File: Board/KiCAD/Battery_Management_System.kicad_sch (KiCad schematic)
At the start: 5 parts, among them J4 Conn_01x02, J5 Conn_01x03, J6 Conn_01x03, J7 Conn_01x05, J8 Conn_01x02

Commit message: Add files via upload
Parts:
- removed J4: Conn_01x02, symbol Connector_Generic:Conn_01x02
- removed J6: Conn_01x03, symbol Connector_Generic:Conn_01x03
- added J1: Conn_01x06_Socket, symbol Connector:Conn_01x06_Socket
- added J9: Conn_01x02, symbol Connector_Generic:Conn_01x02
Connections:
- net Charge Control/VBus: now also J9.1 (Pin_1)
- net GND: now also J1.6 (Pin_6), J9.2 (Pin_2)
- net Microcontroller/USART1_RX: now also J1.2 (Pin_2)
- net Microcontroller/USART1_TX: now also J1.3 (Pin_3)
- new net 3.3V: J1.4 (Pin_4)
- new net NC: J1.1 (Pin_1), J1.5 (Pin_5)
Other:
- sheet Charge Control ports: added none; removed PGND
- sheet Microcontroller ports: added Thermistor C1, Thermistor C2, Thermistor C3, Thermistor C4; removed none
- note added: "External Power In Usercase: 24V/4A"
- note added: "Host Microcontroller"
- note added: "Power out to Load"
- note added: "USB to Serial Breaktout FT232RL"
- note removed: "External Power In Voltage range? Current range?"
- note removed: "Power out, right?"
- note removed: "To Host, right?"
- note removed: "What is this, debug?"
- note removed: "What voltage? Current?"
- moved on the sheet: J5, J7, J8

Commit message: Add files via upload
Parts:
- J1: footprint (none) -> Connector_PinHeader_1.00mm:PinHeader_1x06_P1.00mm_Vertical
- J5: footprint (none) -> Connector_PinHeader_1.00mm:PinHeader_1x03_P1.00mm_Vertical
- J7: footprint (none) -> Connector_PinHeader_1.00mm:PinHeader_1x05_P1.00mm_Vertical
- J8, J9: footprint (none) -> Connector_PinHeader_1.00mm:PinHeader_1x02_P1.00mm_Vertical
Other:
- moved on the sheet: J1, J5, J7, J8, J9

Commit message: Add files via upload
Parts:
- J1: footprint Connector_PinHeader_1.00mm:PinHeader_1x06_P1.00mm_Vertical -> Connector_PinHeader_2.54mm:PinHeader_1x06_P2.54mm_Vertical
- J5: footprint Connector_PinHeader_1.00mm:PinHeader_1x03_P1.00mm_Vertical -> Connector_PinHeader_2.54mm:PinHeader_1x03_P2.54mm_Vertical
- J7: footprint Connector_PinHeader_1.00mm:PinHeader_1x05_P1.00mm_Vertical -> Connector_PinHeader_2.54mm:PinHeader_1x05_P2.54mm_Vertical
- J8, J9: footprint Connector_PinHeader_1.00mm:PinHeader_1x02_P1.00mm_Vertical -> Connector_PinHeader_2.54mm:PinHeader_1x02_P2.54mm_Vertical
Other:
- note removed: "So you're going to use castellated vias, right? How do you do those? A footprint with multiple connector icons?"
- note removed: "User MUST place batteries starting at Cell 1. Unused cells MUST be bypassed on carrier PCB."
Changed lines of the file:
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@@
-		)
-	)
-	(text "User MUST place batteries starting at Cell 1.\nUnused cells MUST be bypassed on carrier PCB.\n"
-		(exclude_from_sim no)
-		(at 232.41 123.19 0)
-		(effects
-			(font
-				(size 1.778 1.778)
-			)
 		)
 	)
@@
 		(exclude_from_sim no)
 		(at 195.58 124.46 0)
-		(effects
-			(font
-				(size 1.27 1.27)
-			)
-		)
-	)
-	(text "So you're going to use castellated vias, right? \nHow do you do those? A footprint with multiple connector icons?"
-		(exclude_from_sim no)
-		(at 121.92 156.21 0)
 		(effects
 			(font
@@
 			)
 		)
-		(property "Footprint" "Connector_PinHeader_1.00mm:PinHeader_1x03_P1.00mm_Vertical"
+		(property "Footprint" "Connector_PinHeader_2.54mm:PinHeader_1x03_P2.54mm_Vertical"
 			(at 62.23 87.63 0)
 			(effects
@@
 			)
 		)
-		(property "Footprint" "Connector_PinHeader_1.00mm:PinHeader_1x06_P1.00mm_Vertical"
+		(property "Footprint" "Connector_PinHeader_2.54mm:PinHeader_1x06_P2.54mm_Vertical"
 			(at 60.96 105.41 0)
 			(effects
@@
 			)
 		)
-		(property "Footprint" "Connector_PinHeader_1.00mm:PinHeader_1x02_P1.00mm_Vertical"
+		(property "Footprint" "Connector_PinHeader_2.54mm:PinHeader_1x02_P2.54mm_Vertical"
 			(at 190.5 55.88 0)
 			(effects
@@
 			)
 		)
-		(property "Footprint" "Connector_PinHeader_1.00mm:PinHeader_1x05_P1.00mm_Vertical"
+		(property "Footprint" "Connector_PinHeader_2.54mm:PinHeader_1x05_P2.54mm_Vertical"
 			(at 189.23 120.65 0)
 			(effects
@@
 			)
 		)
-		(property "Footprint" "Connector_PinHeader_1.00mm:PinHeader_1x02_P1.00mm_Vertical"
+		(property "Footprint" "Connector_PinHeader_2.54mm:PinHeader_1x02_P2.54mm_Vertical"
 			(at 63.5 59.69 0)
 			(effects

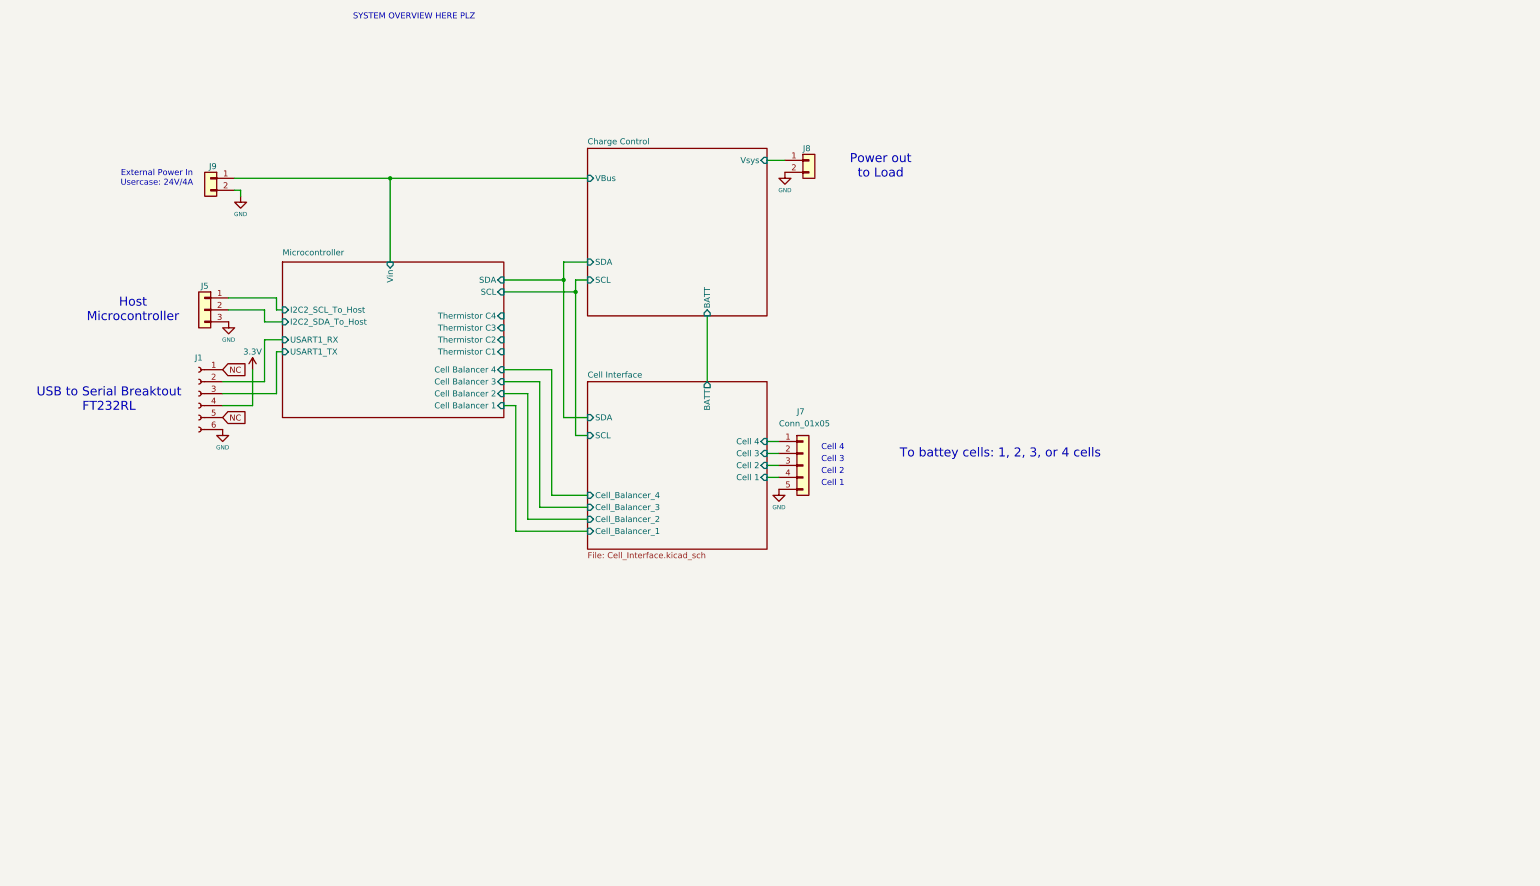
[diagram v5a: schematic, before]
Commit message: Schematic: - Fixed FDI plug - Added thermistor connectors - Added a bunch of NCs using KiCAD NC tool - Added filter cap back into battery current shunt - Added bypass cap to LTC - Removed Cell 4 INA260 because the LTC does current, voltage of that top cell! Board Layout: - Chewed out team for not reading the BQ's datasheet, specifically Section 11 - Relayed out power stream using Section 11 as a refernce - Changed some footprints, mostly reducing size to 0603 - Positioned things optimally given what I thought made sense (dangerous, I know) - Fixed ground planes Other: - Removed PRL and CACHE files from the repo.
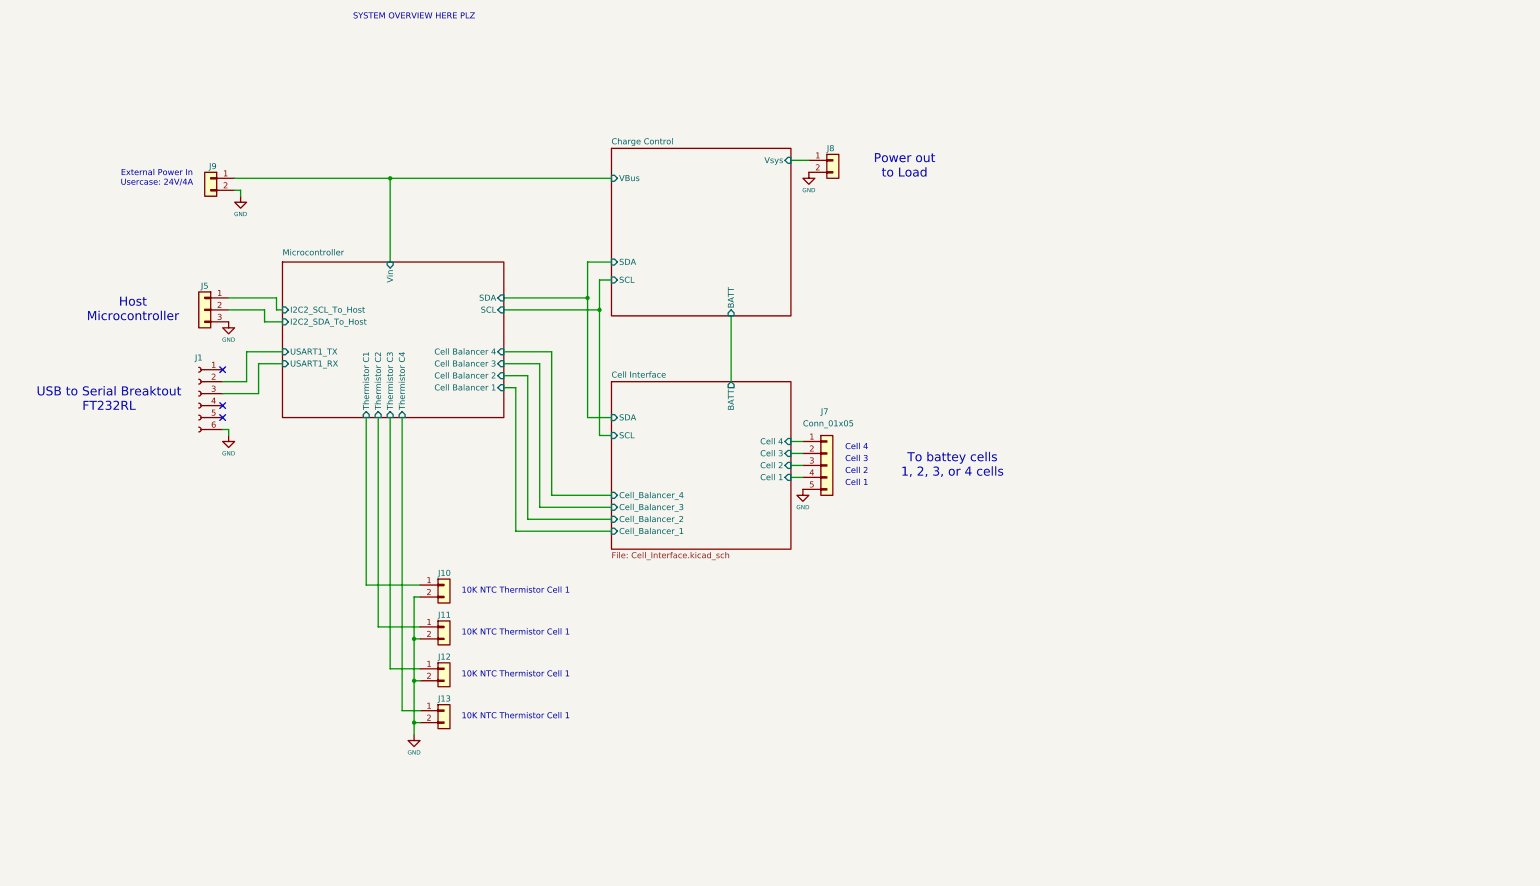
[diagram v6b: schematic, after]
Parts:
- added J10, J11, J12, J13: Conn_01x02, Connector_PinHeader_2.54mm:PinHeader_1x02_P2.54mm_Vertical, symbol Connector_Generic:Conn_01x02
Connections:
- net GND: now also J10.2 (Pin_2), J11.2 (Pin_2), J12.2 (Pin_2), J13.2 (Pin_2)
- net Microcontroller/Thermistor C1: now also J10.1 (Pin_1)
- net Microcontroller/Thermistor C2: now also J11.1 (Pin_1)
- net Microcontroller/Thermistor C3: now also J12.1 (Pin_1)
- net Microcontroller/Thermistor C4: now also J13.1 (Pin_1)
- net Microcontroller/USART1_RX: now also J1.3 (Pin_3); no longer J1.2 (Pin_2)
- net Microcontroller/USART1_TX: now also J1.2 (Pin_2); no longer J1.3 (Pin_3)
- net 3.3V: no longer names the net of J1.4 (Pin_4)
- net NC: no longer names the net of J1.1 (Pin_1)
- net NC: no longer J1.5 (Pin_5)
- no-connect marks 0 -> 3
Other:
- note added: "10K NTC Thermistor Cell 1"
- note added: "To battey cells 1, 2, 3, or 4 cells"
- note removed: "To battey cells: 1, 2, 3, or 4 cells"
- moved on the sheet: J7, J8

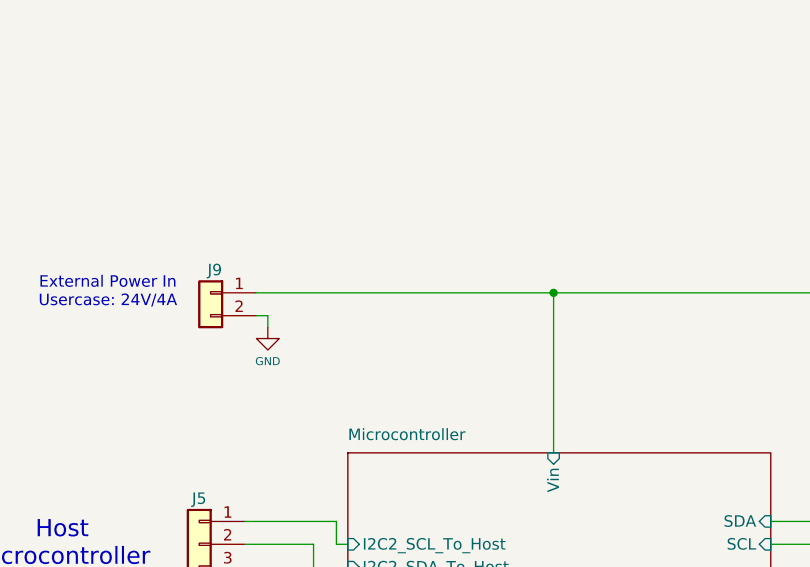
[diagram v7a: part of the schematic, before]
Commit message: Added example test point
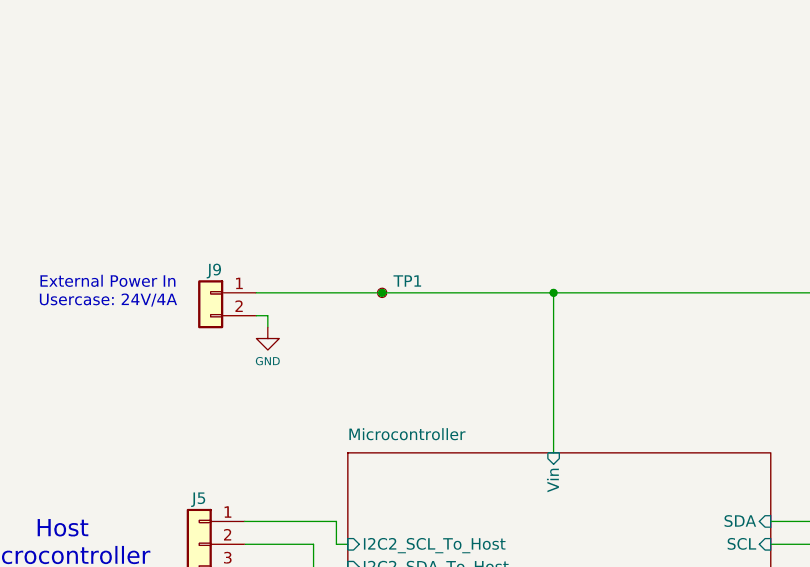
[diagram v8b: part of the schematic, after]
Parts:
- added TP1: TestPoint_Small, TestPoint:TestPoint_THTPad_1.0x1.0mm_Drill0.5mm, symbol Connector:TestPoint_Small
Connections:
- net Charge Control/VBus: now also TP1.1
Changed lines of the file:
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@@
+	)
+	(junction
+		(at 82.55 59.69)
+		(diameter 0)
+		(color 0 0 0 0)
 	)
 	(junction
@@
 	(wire
 		(pts
-			(xy 68.58 59.69) (xy 101.6 59.69)
+			(xy 68.58 59.69) (xy 82.55 59.69)
 		)
 		(stroke
@@
 		(pts
 			(xy 106.68 148.59) (xy 106.68 157.48)
+		)
+		(stroke
+			(width 0)
+			(type default)
+		)
+	)
+	(wire
+		(pts
+			(xy 82.55 59.69) (xy 101.6 59.69)
 		)
 		(stroke
@@
 					(unit 1)
 				)
+			)
+		)
+	)
+	(symbol
+		(lib_id "Connector:TestPoint_Small")
+		(at 82.55 59.69 0)
+		(unit 1)
+		(exclude_from_sim no)
+		(in_bom no)
+		(on_board yes)
+		(dnp no)
+		(fields_autoplaced yes)
+		(property "Reference" "TP1"
+			(at 83.82 58.4199 0)
+			(effects
+				(font
+					(size 1.27 1.27)
+				)
+				(justify left)
+			)
+		)
+		(property "Value" "TestPoint_Small"
+			(at 83.82 60.9599 0)
+			(effects
+				(font
+					(size 1.27 1.27)
+				)
+				(justify left)
+				(hide yes)
+			)
+		)
+		(property "Footprint" "TestPoint:TestPoint_THTPad_1.0x1.0mm_Drill0.5mm"
+			(at 87.63 59.69 0)
+			(effects
+				(font
+					(size 1.27 1.27)
+				)
+				(hide yes)
+			)
+		)
+		(property "Datasheet" "~"
+			(at 87.63 59.69 0)
+			(effects
+				(font
+					(size 1.27 1.27)
+				)
+				(hide yes)
+			)
+		)
+		(property "Description" "test point"
+			(at 82.55 59.69 0)
+			(effects
+				(font
+					(size 1.27 1.27)
+				)
+				(hide yes)
+			)
+		)
+		(pin "1"
+		)
+		(instances
+			(project ""
+				(path "/1ea1a1f5-2618-4570-85b6-e164c8f0e76f"
+					(reference "TP1")
+					(unit 1)
+				)
